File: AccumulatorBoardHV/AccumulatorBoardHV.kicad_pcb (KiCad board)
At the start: 2 copper layers, 179.7 x 69.2 mm, 48 parts, among them J1 TS -> GLV Regulator Jumper, J10 Charger Current, J2 To LV Board, J3 Batt Voltage, J4 TS (Switched), J5 IMD TS, J6 To LV Board, J7 Acc LED 1, J8 Acc LED 2, J9 Charger Current to Batt, U1 V110C12E100BL, U2 DK1A1B-12V, U3 RDD08110S3V3, U4 PS2501-4, U5 G2RL-1A-E, U6 G2RL-1A-E

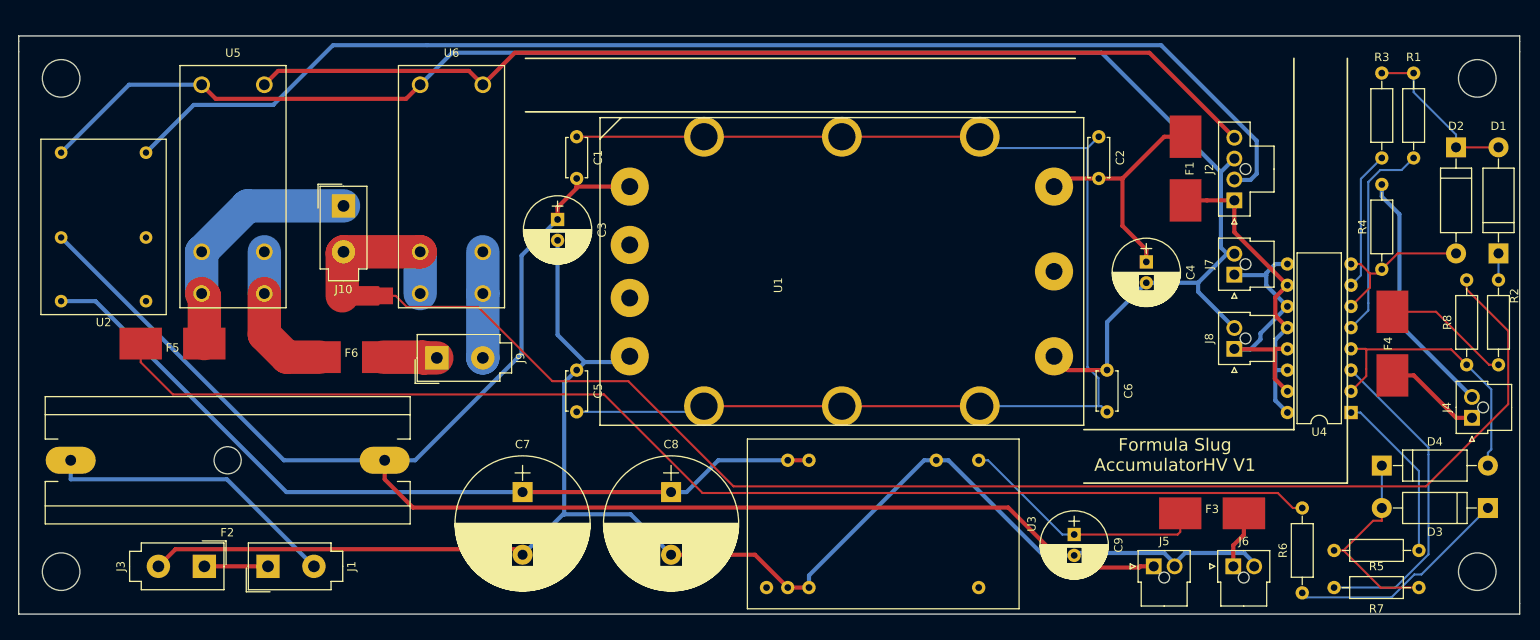
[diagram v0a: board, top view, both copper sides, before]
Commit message: Revise boards based on design review
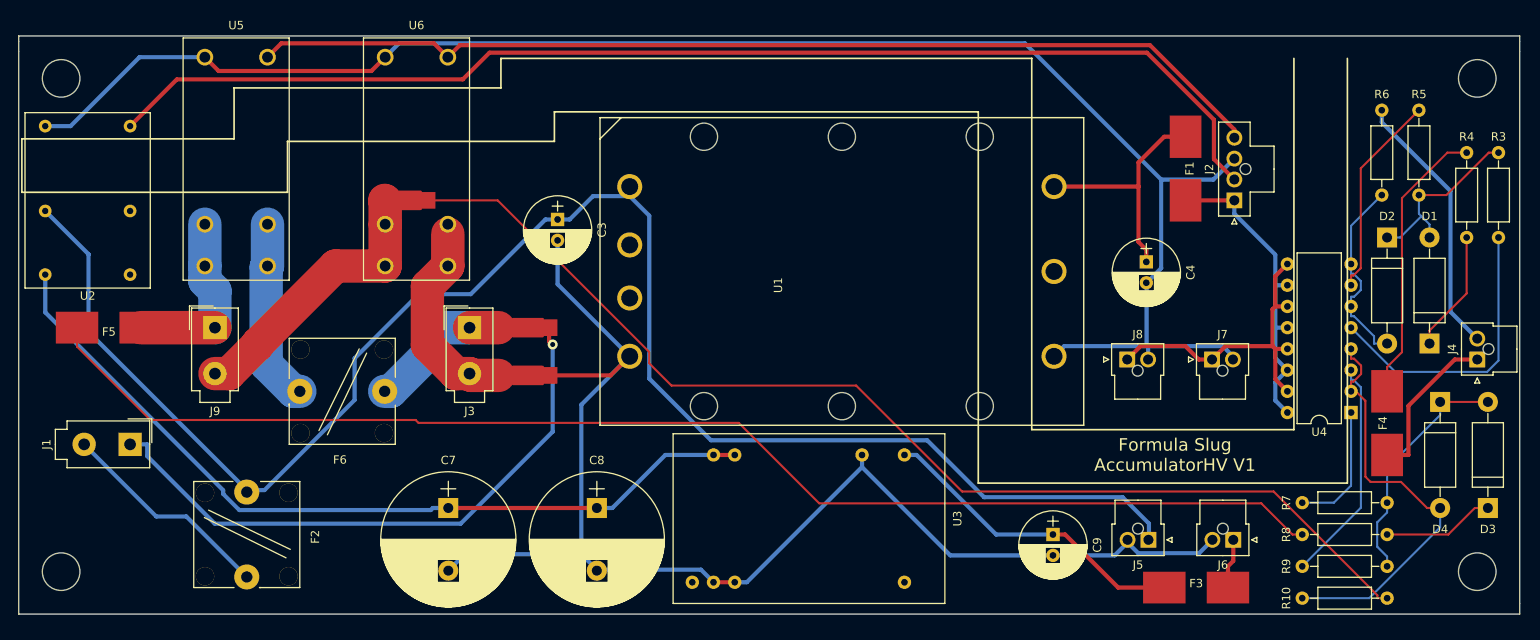
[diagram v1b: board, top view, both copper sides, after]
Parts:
- removed C1, C2, C5, C6: C, Capacitors_THT:C_Disc_D4.7mm_W2.5mm_P5.00mm
- removed J10: Charger Current, Connectors_Molex:Molex_MiniFit-JR-5556-02A_2x01x4.20mm_Straight
- added R10: 1.5kR, Resistors_THT:R_Axial_DIN0207_L6.3mm_D2.5mm_P10.16mm_Horizontal, F.Cu at (177.2, 98.4)
- added R11: 0, FSFootprints:SMDNetTie, F.Cu at (69.8, 50.8)
- F2: footprint Fuse_Holders_and_Fuses:Fuseholder6x32_Horiz_Open_Schurter0031-8002 -> Fuse_Holders_and_Fuses:Fuseholder5x20_vert_closed_Bulgin_FX0456
- F6: value Fuse -> Charger Fuse; footprint FSFootprints:SMD Fuse -> Fuse_Holders_and_Fuses:Fuseholder5x20_vert_closed_Bulgin_FX0456
- J9: value Charger Current to Batt -> Charger Current
- R1: value R -> 0; footprint Resistors_THT:R_Axial_DIN0207_L6.3mm_D2.5mm_P10.16mm_Horizontal -> FSFootprints:SMDNetTie
- R2: value 1.5kR -> 0; footprint Resistors_THT:R_Axial_DIN0207_L6.3mm_D2.5mm_P10.16mm_Horizontal -> FSFootprints:SMDNetTie
- R9: value 0 -> R; footprint Oddities:NetTie-I_Connected_SMD -> Resistors_THT:R_Axial_DIN0207_L6.3mm_D2.5mm_P10.16mm_Horizontal
- U1: footprint FSFootprints:VICOR-DCDC -> FSFootprints:Vicor_Micro
- moved R9 117.0 mm to (177.2, 94.6), turned to 0 degrees
- moved R2 116.8 mm to (84.5, 71.8), turned to 180 degrees
- moved R1 108.0 mm to (84.5, 66.0), turned to 180 degrees
- moved R5 52.7 mm to (191.1, 40.0), turned to 270 degrees
- moved R6 48.6 mm to (186.7, 50.2)
- moved J3 42.7 mm to (77.5, 66.0), turned to 0 degrees
- moved J9 26.8 mm to (47.0, 66.0), turned to 0 degrees
- moved R8 22.4 mm to (187.3, 90.8), turned to 180 degrees
- moved J1 22.0 mm to (36.8, 80.0), turned to 270 degrees
- moved F2 16.9 mm to (50.8, 85.7), turned to 270 degrees
- moved R3 16.9 mm to (200.7, 55.2)
- moved D2 13.6 mm to (187.3, 55.2)
- moved D1 13.6 mm to (192.4, 67.9)
- moved J8 12.9 mm to (156.2, 69.8), turned to 0 degrees
- moved R4 10.9 mm to (196.8, 55.2)
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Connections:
- net Net-(C9-Pad1) renamed /3.3V_TS_PRE
- J3 pad 1: /BATT+_DIRECT -> /BATT+_CHARGER
- J3 pad 2: /BATT- -> /BATT-_CHARGER
- J9 pad 1: /BATT+_CHARGER -> /CHARGER+
- J9 pad 2: /BATT-_CHARGER -> /CHARGER-
- R1 pad 1: Net-(R1-Pad1) -> /BATT+_DIRECT
- R1 pad 2: Net-(D1-Pad2) -> /BATT+_CHARGER
- R2 pad 1: Net-(D1-Pad1) -> /BATT-
- R2 pad 2: Net-(F4-Pad1) -> /BATT-_CHARGER
- R4 pad 1: Net-(D2-Pad2) -> Net-(D1-Pad1)
- R4 pad 2: /TS- -> Net-(F4-Pad1)
- R5 pad 2: Net-(D3-Pad2) -> Net-(D1-Pad2)
- R6 pad 1: Net-(D3-Pad1) -> Net-(D2-Pad2)
- R6 pad 2: Net-(F5-Pad1) -> /TS-
- R8 pad 1: Net-(D4-Pad2) -> Net-(D3-Pad1)
- R8 pad 2: Net-(R8-Pad2) -> Net-(F5-Pad1)
- R9 pad 1: Net-(R8-Pad2) -> Net-(R9-Pad1)
- R9 pad 2: /CHARGER- -> Net-(D3-Pad2)
- U4 pad 1: Net-(R5-Pad1) -> Net-(R7-Pad1)
- U4 pad 3: Net-(R7-Pad1) -> Net-(R9-Pad1)
- U4 pad 5: Net-(R1-Pad1) -> Net-(R3-Pad1)
- U4 pad 7: Net-(R3-Pad1) -> Net-(R5-Pad1)
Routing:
- net Net-(R8-Pad2): track 165.0 -> 0.00 mm
- net Net-(C1-Pad1): track 159.1 -> 0.00 mm
- net Net-(R10-Pad2): track 0.00 -> 135.7 mm
- net /BATT+_DIRECT: track 7.62 -> 72.6 mm, vias 0 -> 1
- net /BATT-: track 193.1 -> 161.6 mm
- net Net-(R9-Pad1): track 0.00 -> 27.1 mm
- net Net-(R1-Pad1): track 24.9 -> 0.00 mm
- net Net-(R7-Pad1): track 38.9 -> 15.4 mm
- net Net-(F4-Pad1): track 15.3 -> 33.9 mm
- net Net-(R3-Pad1): track 16.8 -> 35.1 mm
- net Net-(D4-Pad2): track 33.9 -> 50.8 mm
- net /CHARGER-: track 19.5 -> 33.7 mm
- net /BATT-_CHARGER: track 12.7 -> 26.5 mm
- net Net-(D3-Pad1): track 26.9 -> 13.4 mm
- net /BATT+_CHARGER: track 6.46 -> 19.3 mm
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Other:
- net class ChgCurrent: clearance 0.2 -> 1
- net class Default: clearance 0.2 -> 0.24
- rule trace_clearance: 0.2 -> 0.24

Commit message: update some footprint throughole sizes
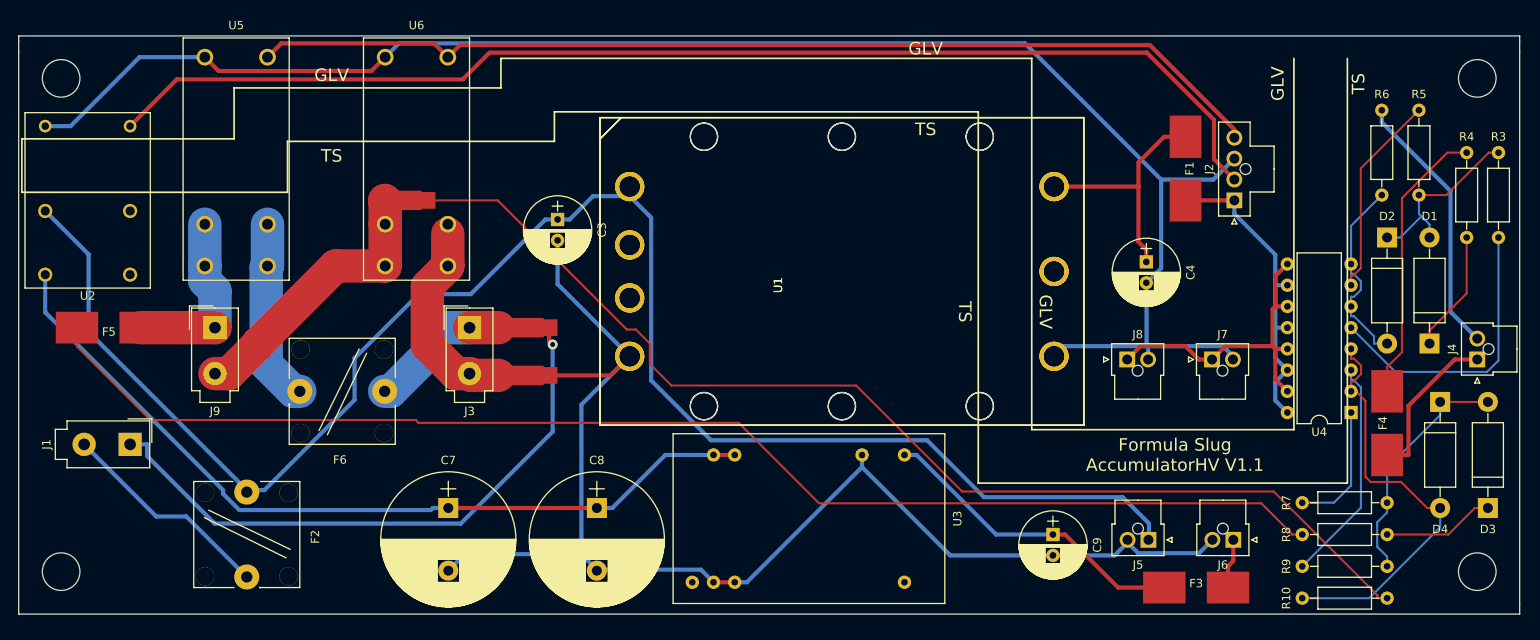
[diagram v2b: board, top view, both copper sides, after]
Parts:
- added U1: V110C12E100BL, FSFootprints:Vicor_Micro, F.Cu at (96.6, 43.2)
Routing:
- net Net-(R10-Pad2): track 135.7 -> 136.3 mm
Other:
- board text added: "Formula Slug AccumulatorHV V1.1"
- board text added: "GLV TS"
- board text removed: "Formula Slug AccumulatorHV V1"

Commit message: shrink AccumulatorHV PCB
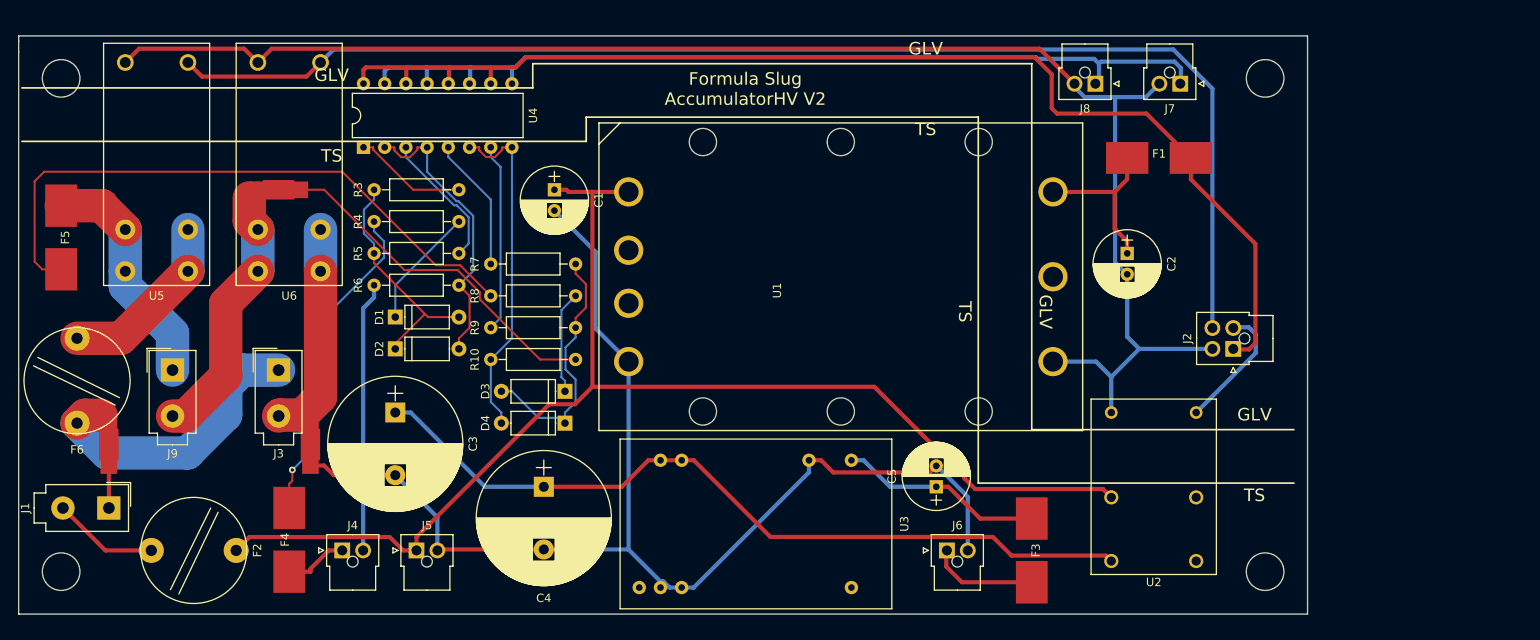
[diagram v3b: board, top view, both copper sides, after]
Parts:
- removed C7, C8: 100uF, Capacitors_THT:CP_Radial_D16.0mm_P7.50mm
- removed C9: CP, Capacitors_THT:CP_Radial_D8.0mm_P2.50mm
- removed the U1 at (96.6, 43.2) (x2)
- added C1: 0.47uF, Capacitors_THT:CP_Radial_D8.0mm_P2.50mm, F.Cu at (87.6, 49.5)
- added C2: CP, Capacitors_THT:CP_Radial_D8.0mm_P2.50mm, F.Cu at (156.2, 57.1)
- added C5: CP, Capacitors_THT:CP_Radial_D8.0mm_P2.50mm, F.Cu at (133.3, 85.1)
- added U1: V110C12E100BL, FSFootprints:Vicor_Micro, F.Cu at (96.5, 43.8)
- C3: value 0.47uF -> 100uF; footprint Capacitors_THT:CP_Radial_D8.0mm_P2.50mm -> Capacitors_THT:CP_Radial_D16.0mm_P7.50mm
- C4: value CP -> 100uF; footprint Capacitors_THT:CP_Radial_D8.0mm_P2.50mm -> Capacitors_THT:CP_Radial_D16.0mm_P7.50mm
- D1, D2, D3, D4: footprint Diodes_THT:D_DO-15_P12.70mm_Horizontal -> Diodes_THT:D_A-405_P7.62mm_Horizontal
- F2, F6: footprint Fuse_Holders_and_Fuses:Fuseholder5x20_vert_closed_Bulgin_FX0456 -> FSFootprints:Fuseholder5x20_vert
- J2: footprint Connectors_Molex:Molex_NanoFit_1x04x2.50mm_Straight -> Connectors_Molex:Molex_NanoFit_2x02x2.50mm_Straight
- U4: value PS2501-4 -> PS2501-4-1
- moved J4 137.8 mm to (62.2, 92.7), turned to 0 degrees
- moved F4 132.2 mm to (55.9, 91.4)
- moved U2 132.2 mm to (159.4, 86.4)
- moved R3 124.6 mm to (76.2, 49.5), turned to 180 degrees
- moved D1 123.9 mm to (68.6, 64.8), turned to 0 degrees
- moved U4 122.4 mm to (64.8, 44.5), turned to 90 degrees
- moved R4 120.7 mm to (76.2, 53.3), turned to 180 degrees
- moved D2 119.5 mm to (68.6, 68.6), turned to 0 degrees
- moved R5 116.2 mm to (76.2, 57.1), turned to 180 degrees
- moved D3 111.4 mm to (88.9, 73.7), turned to 180 degrees
- moved R6 111.0 mm to (76.2, 61.0), turned to 180 degrees
- moved D4 104.8 mm to (88.9, 77.5), turned to 180 degrees
- moved R10 101.3 mm to (80.0, 69.8)
- moved R7 101.3 mm to (80.0, 58.4)
- moved R8 101.3 mm to (90.2, 62.2)
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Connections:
- C3 pad 1: /BATT+ -> /BATT+_LVBOARD
- C4 pad 1: /VICOR_OUT -> /BATT+_LVBOARD
- C4 pad 2: GND -> /BATT-
- U4 pad 1: Net-(R7-Pad1) -> Net-(R3-Pad1)
- U4 pad 2: Net-(D4-Pad2) -> Net-(D2-Pad2)
- U4 pad 3: Net-(R9-Pad1) -> Net-(R5-Pad1)
- U4 pad 4: Net-(D4-Pad2) -> Net-(D2-Pad2)
- U4 pad 5: Net-(R3-Pad1) -> Net-(R7-Pad1)
- U4 pad 6: Net-(D2-Pad2) -> Net-(D4-Pad2)
- U4 pad 7: Net-(R5-Pad1) -> Net-(R9-Pad1)
- U4 pad 8: Net-(D2-Pad2) -> Net-(D4-Pad2)
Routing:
- net /12V: track 144.9 -> 15.4 mm
- net /12V_SRC: track 38.0 -> 143.6 mm
- net Net-(R10-Pad2): track 136.3 -> 41.9 mm
- net Net-(F5-Pad1): track 158.3 -> 74.4 mm
- net /12V_INDICATOR: track 39.0 -> 108.6 mm
- net /BATT+_DIRECT: track 72.6 -> 5.08 mm, vias 1 -> 0
- net /BATT+: track 199.9 -> 153.1 mm
- net /AIRS_FINAL_CHARGER: track 122.9 -> 155.3 mm
- net Net-(R3-Pad1): track 35.1 -> 13.7 mm
- net /BATT+_CHARGER: track 19.3 -> 36.3 mm
- net GND: track 200.8 -> 186.0 mm
- net /BATT-: track 161.6 -> 148.2 mm
- net /BATT+_DIRFUSED: track 26.0 -> 12.7 mm
- net /3.3V_TS_PRE: track 37.7 -> 24.5 mm
- net /TS+: track 19.0 -> 7.60 mm
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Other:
- board size 179.7 x 69.2 mm -> 154.3 x 69.2 mm
- net class ChgCurrent: via_dia 3.2 -> 100
- board text added: "Formula Slug AccumulatorHV V2"
- board text removed: "Formula Slug AccumulatorHV V1.1"

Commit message: Tweak 60v circuits based on testing results
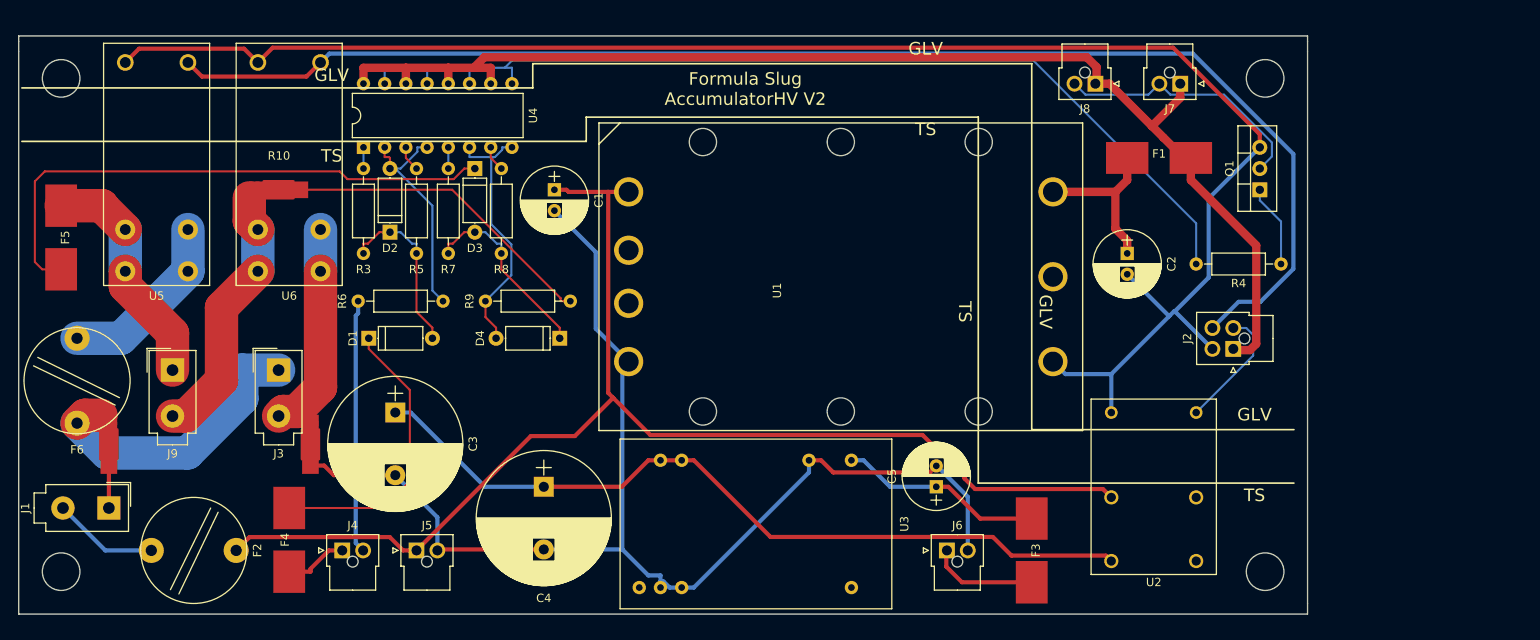
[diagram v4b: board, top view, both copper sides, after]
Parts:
- removed R11: 0, FSFootprints:SMDNetTie
- added Q1: Q_NMOS_GDS, TO_SOT_Packages_THT:TO-220-3_Vertical, F.Cu at (172.1, 49.5)
- D1, D3: value 48V Zener -> 56V Zener
- R10: value 1.5kR -> 0; footprint Resistors_THT:R_Axial_DIN0207_L6.3mm_D2.5mm_P10.16mm_Horizontal -> FSFootprints:SMDNetTie
- R3, R5, R7: value R -> 1.2k
- R4: value 1.5kR -> 100
- R6: value 1.5kR -> 1.5k
- R8: value 1.5kR -> 1.2k
- R9: value R -> 1.5k
- moved R4 98.6 mm to (174.6, 58.4)
- moved R10 32.5 mm to (54.6, 49.5), turned to 180 degrees
- moved D3 28.8 mm to (78.1, 47.0), turned to 270 degrees
- moved R8 17.6 mm to (81.3, 47.0), turned to 270 degrees
- moved D2 14.0 mm to (67.9, 54.6), turned to 90 degrees
- moved R7 12.5 mm to (74.9, 47.0), turned to 270 degrees
- moved R3 11.7 mm to (64.8, 47.0), turned to 270 degrees
- moved R5 11.4 mm to (71.1, 47.0), turned to 270 degrees
- moved D4 10.2 mm to (88.3, 67.3)
- moved D1 4.07 mm to (65.4, 67.3)
- moved R9 3.24 mm to (79.4, 62.9)
- moved R6 2.69 mm to (74.3, 62.9)
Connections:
- F4 pad 1: Net-(F4-Pad1) -> Net-(D1-Pad1)
- F5 pad 1: Net-(F5-Pad1) -> Net-(D3-Pad1)
- J7 pad 1: /12V_INDICATOR -> /12V_SRC
- J7 pad 2: GND -> /12V_INDICATOR
- J8 pad 1: /12V_INDICATOR -> /12V_SRC
- J8 pad 2: GND -> /12V_INDICATOR
- R10 pad 1: Net-(D4-Pad2) -> Net-(R10-Pad1)
- R10 pad 2: Net-(R10-Pad2) -> /CHARGER-
- R4 pad 1: Net-(D1-Pad1) -> Net-(Q1-Pad1)
- R4 pad 2: Net-(F4-Pad1) -> /12V_INDICATOR_CTRL
- R8 pad 1: Net-(D3-Pad1) -> Net-(R8-Pad1)
- R8 pad 2: Net-(F5-Pad1) -> Net-(D3-Pad2)
- R9 pad 1: Net-(R9-Pad1) -> Net-(D4-Pad2)
- R9 pad 2: Net-(D3-Pad2) -> Net-(R10-Pad1)
- U4 pad 11: /12V_INDICATOR -> /12V_INDICATOR_CTRL
- U4 pad 13: /12V_INDICATOR -> /12V_INDICATOR_CTRL
- U4 pad 15: /12V_INDICATOR -> /12V_INDICATOR_CTRL
- U4 pad 7: Net-(R9-Pad1) -> Net-(R8-Pad1)
- U4 pad 9: /12V_INDICATOR -> /12V_INDICATOR_CTRL
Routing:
- net /12V_INDICATOR_CTRL: track 0.00 -> 118.9 mm
- net /12V_INDICATOR: track 108.6 -> 31.4 mm
- net Net-(F5-Pad1): track 74.4 -> 0.00 mm
- net Net-(D3-Pad1): track 12.3 -> 67.2 mm
- net Net-(R10-Pad2): track 41.9 -> 0.00 mm
- net Net-(F4-Pad1): track 39.5 -> 0.00 mm, vias 1 -> 0
- net Net-(R10-Pad1): track 0.00 -> 38.1 mm
- net Net-(R9-Pad1): track 22.6 -> 0.00 mm
- net Net-(D1-Pad1): track 14.6 -> 34.9 mm
- net GND: track 186.0 -> 204.0 mm
- net Net-(R7-Pad1): track 16.1 -> 2.54 mm
- net Net-(R5-Pad1): track 16.5 -> 3.07 mm
- net Net-(R3-Pad1): track 13.7 -> 2.54 mm
- net /AIRS_FINAL_CHARGER: track 155.3 -> 165.5 mm
- net Net-(Q1-Pad1): track 0.00 -> 9.94 mm
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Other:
- net class Source added: clearance 0.24, trace_width 1, via_dia 1.6, via_drill 0.9
